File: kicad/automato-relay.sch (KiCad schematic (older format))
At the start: 26 parts, among them J1 Screw_Terminal_01x02, J2 Screw_Terminal_01x02, J3 Screw_Terminal_01x02, J4 Screw_Terminal_01x05, J5 Screw_Terminal_01x02, J6 Screw_Terminal_01x02, J7 Screw_Terminal_01x05, J8 Screw_Terminal_01x02, K1 G5LE-14, K2 G5LE-14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

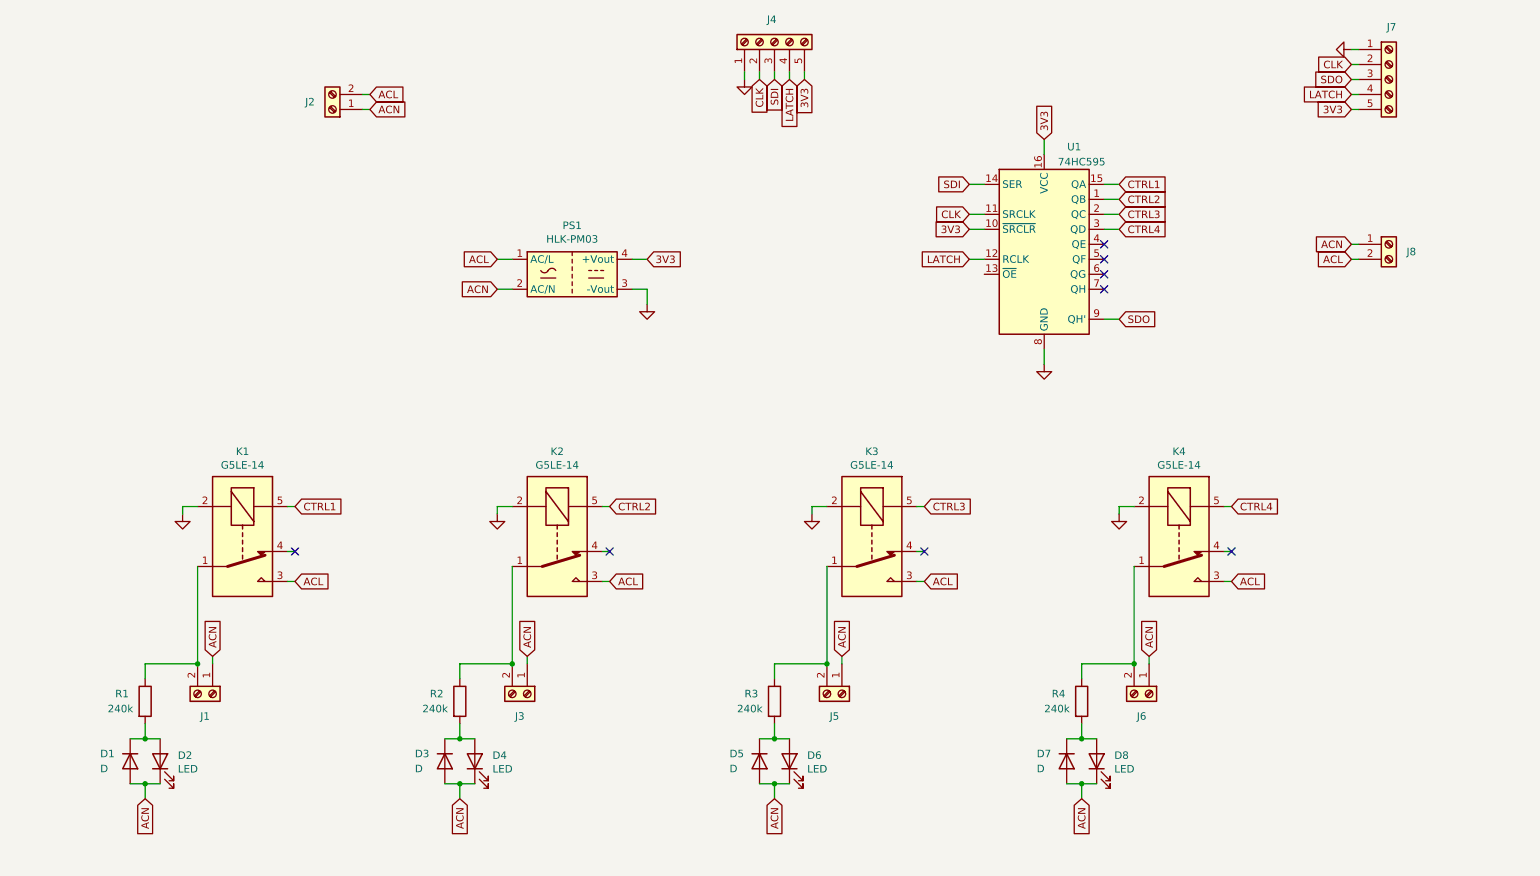
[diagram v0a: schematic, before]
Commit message: add low-side mosfets for relay coils
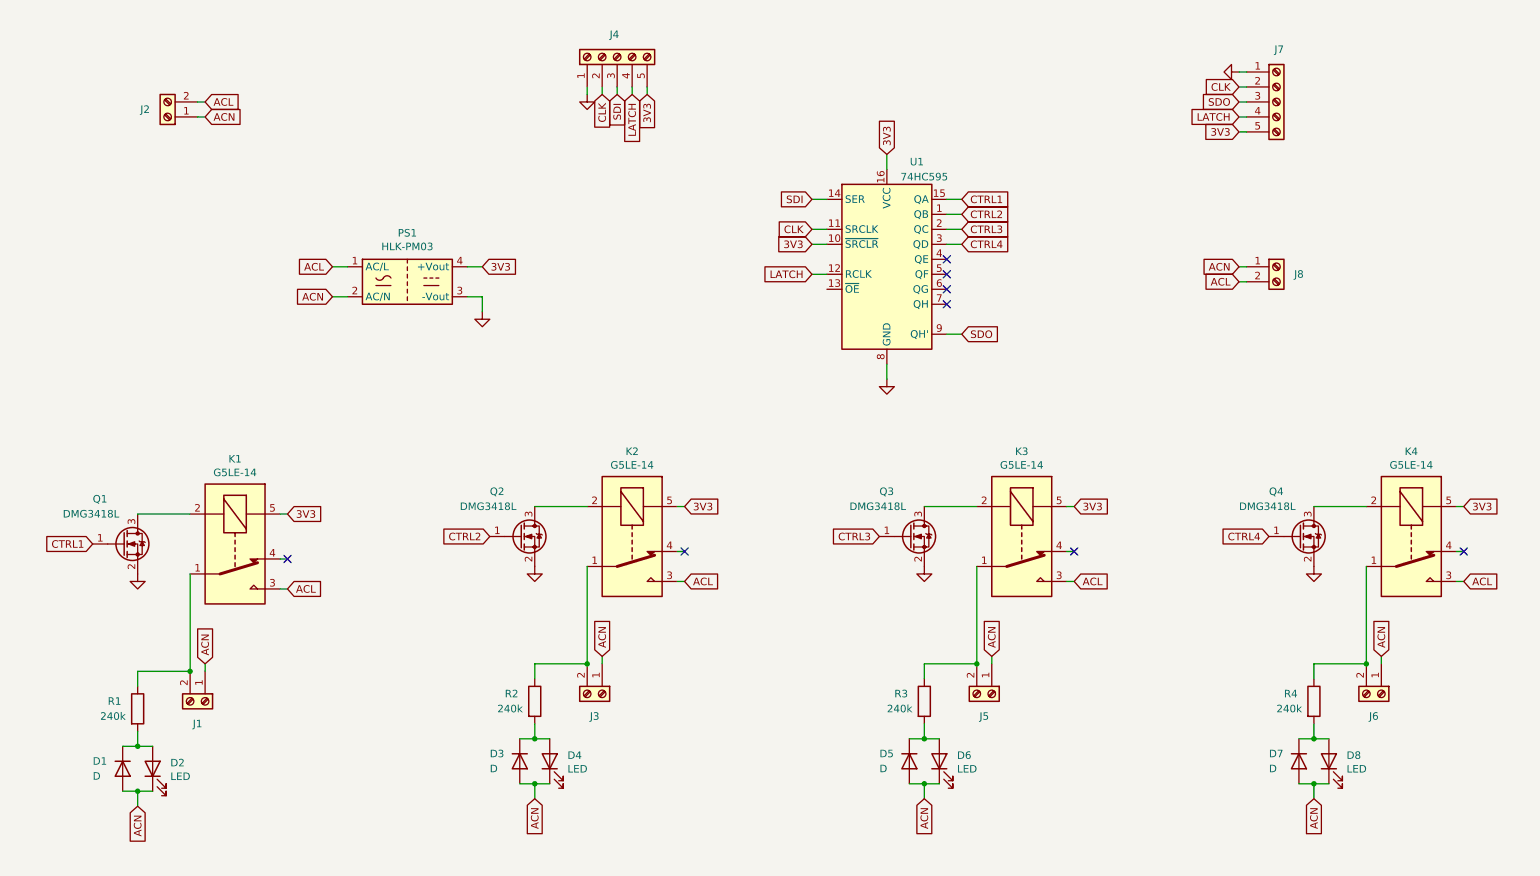
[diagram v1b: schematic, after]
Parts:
- added Q1, Q2, Q3, Q4: DMG3418L, Package_TO_SOT_SMD:SOT-23, symbol Transistor_FET:DMG3418L
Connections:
- net 3V3: now also K1.5, K2.5, K3.5, K4.5
- net CTRL1: now also Q1.1 (G); no longer K1.5
- net CTRL2: now also Q2.1 (G); no longer K2.5
- net CTRL3: now also Q3.1 (G); no longer K3.5
- net CTRL4: now also Q4.1 (G); no longer K4.5
- net GND: now also Q1.2 (S), Q2.2 (S), Q3.2 (S), Q4.2 (S); no longer K1.2, K2.2, K3.2, K4.2
- new net: K1.2, Q1.3 (D)
- new net: K2.2, Q2.3 (D)
- new net: K3.2, Q3.3 (D)
- new net: K4.2, Q4.3 (D)
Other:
- moved on the sheet: D1, D2, D3, D4, D5, D6, D7, D8, J1, J2, J3, J4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

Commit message: add earth ground connections
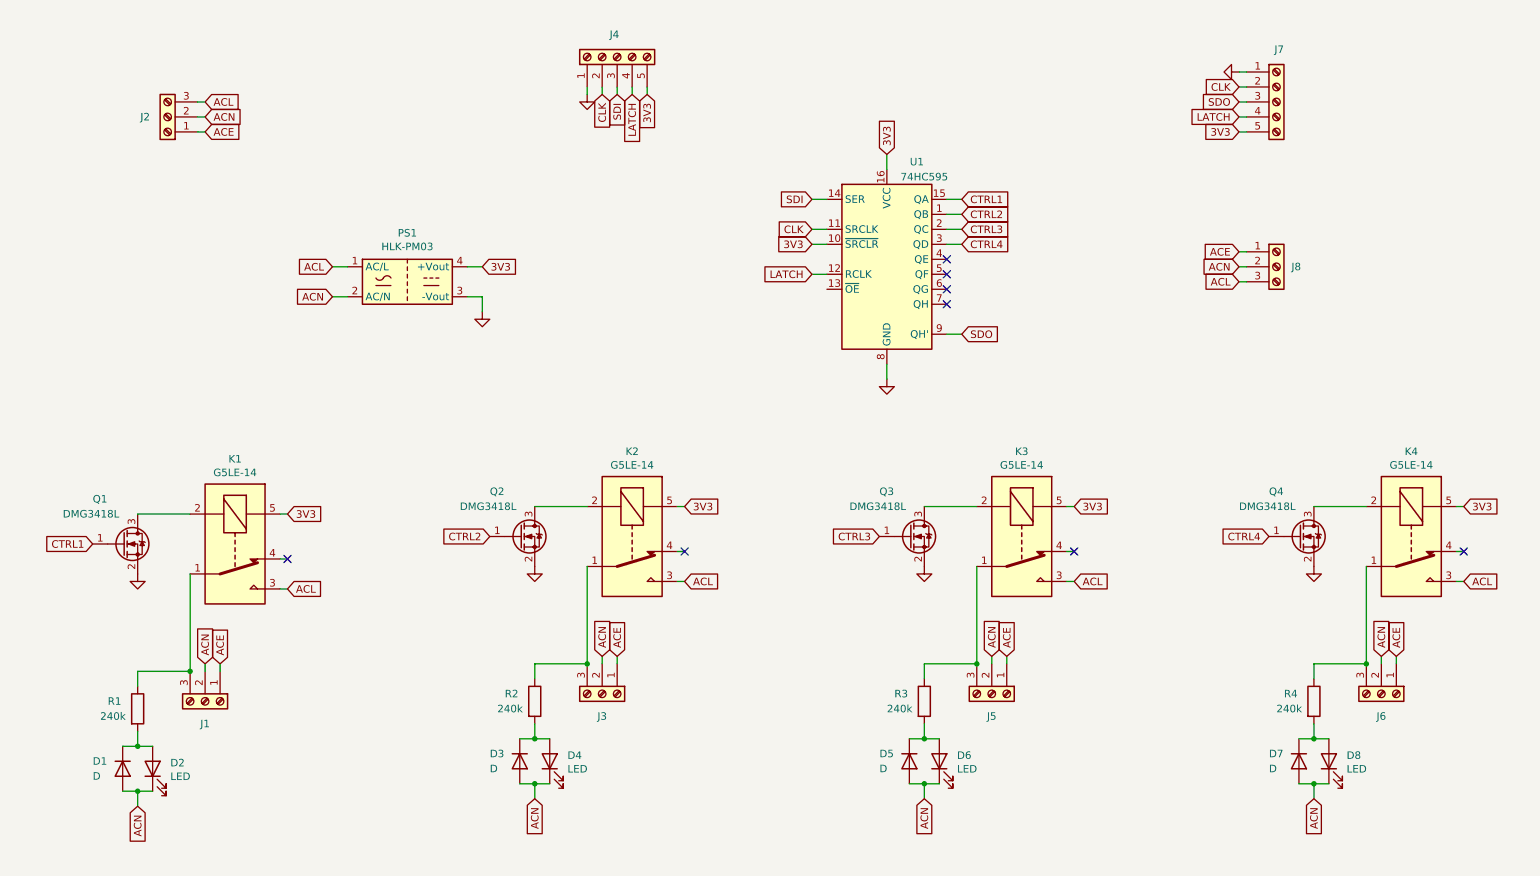
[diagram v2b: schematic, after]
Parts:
- removed J1, J2, J3, J5, J6, J8: Screw_Terminal_01x02, symbol Connector:Screw_Terminal_01x02
- added J1, J2, J3, J5, J6, J8: Screw_Terminal_01x03, symbol Connector:Screw_Terminal_01x03
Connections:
- net ACL: now also J2.3 (Pin_3), J8.3 (Pin_3)
- net ACN: now also J1.2 (Pin_2), J2.2 (Pin_2), J3.2 (Pin_2), J5.2 (Pin_2), J6.2 (Pin_2), J8.2 (Pin_2)
- net at K1.1, R1.1: now also J1.3 (Pin_3)
- net at K2.1, R2.1: now also J3.3 (Pin_3)
- net at K3.1, R3.1: now also J5.3 (Pin_3)
- net at K4.1, R4.1: now also J6.3 (Pin_3)
- new net ACE: J1.1 (Pin_1), J2.1 (Pin_1), J3.1 (Pin_1), J5.1 (Pin_1), J6.1 (Pin_1), J8.1 (Pin_1)
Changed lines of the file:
@@
 Wire Wire Line
 	3800 2350 3900 2350
-$Comp
-L Connector:Screw_Terminal_01x02 J2
-U 1 1 60248A15
-P 1800 1350
-F 0 "J2" H 1950 1300 50  0000 C CNN
-F 1 "Screw_Terminal_01x02" H 2350 1350 50  0001 C CNN
-F 2 "" H 1800 1350 50  0001 C CNN
-F 3 "~" H 1800 1350 50  0001 C CNN
-	1    1800 1350
-	-1   0    0    1
-$EndComp
 Text GLabel 2900 2550 0    50   Input ~ 0
 ACN
 Text GLabel 2050 5000 1    50   Input ~ 0
 ACN
-$Comp
-L Connector:Screw_Terminal_01x02 J1
-U 1 1 6025D31A
-P 2050 5250
-F 0 "J1" V 2200 5200 50  0000 C CNN
-F 1 "Screw_Terminal_01x02" H 2050 5000 50  0001 C CNN
-F 2 "" H 2050 5250 50  0001 C CNN
-F 3 "~" H 2050 5250 50  0001 C CNN
-	1    2050 5250
-	0    1    1    0
-$EndComp
 Wire Wire Line
 	2900 2550 3000 2550
@@
 Text GLabel 4700 4950 1    50   Input ~ 0
 ACN
-$Comp
-L Connector:Screw_Terminal_01x02 J3
-U 1 1 603390E0
-P 4700 5200
-F 0 "J3" V 4850 5150 50  0000 C CNN
-F 1 "Screw_Terminal_01x02" H 4700 4950 50  0001 C CNN
-F 2 "" H 4700 5200 50  0001 C CNN
-F 3 "~" H 4700 5200 50  0001 C CNN
-	1    4700 5200
-	0    1    1    0
-$EndComp
 Wire Wire Line
 	4700 4950 4700 5000
@@
 Wire Wire Line
 	4600 4350 4600 5000
-Connection ~ 4600 5000
 $Comp
 L automato-relay:G5LE-14 K3
@@
 Text GLabel 7300 4950 1    50   Input ~ 0
 ACN
-$Comp
-L Connector:Screw_Terminal_01x02 J5
-U 1 1 603475EE
-P 7300 5200
-F 0 "J5" V 7450 5150 50  0000 C CNN
-F 1 "Screw_Terminal_01x02" H 7300 4950 50  0001 C CNN
-F 2 "" H 7300 5200 50  0001 C CNN
-F 3 "~" H 7300 5200 50  0001 C CNN
-	1    7300 5200
-	0    1    1    0
-$EndComp
 Wire Wire Line
 	7300 4950 7300 5000
@@
 Wire Wire Line
 	7200 4350 7200 5000
-Connection ~ 7200 5000
 $Comp
 L automato-relay:G5LE-14 K4
@@
 Text GLabel 9900 4950 1    50   Input ~ 0
 ACN
-$Comp
-L Connector:Screw_Terminal_01x02 J6
-U 1 1 60347654
-P 9900 5200
-F 0 "J6" V 10050 5150 50  0000 C CNN
-F 1 "Screw_Terminal_01x02" H 9900 4950 50  0001 C CNN
-F 2 "" H 9900 5200 50  0001 C CNN
-F 3 "~" H 9900 5200 50  0001 C CNN
-	1    9900 5200
-	0    1    1    0
-$EndComp
 Wire Wire Line
 	9900 4950 9900 5000
@@
 Wire Wire Line
 	9800 4350 9800 5000
-Connection ~ 9800 5000
-$Comp
-L Connector:Screw_Terminal_01x02 J8
-U 1 1 603A21E6
-P 9200 2350
-F 0 "J8" H 9350 2300 50  0000 C CNN
-F 1 "Screw_Terminal_01x02" H 9750 2350 50  0001 C CNN
-F 2 "" H 9200 2350 50  0001 C CNN
-F 3 "~" H 9200 2350 50  0001 C CNN
-	1    9200 2350
-	1    0    0    -1
-$EndComp
 Text GLabel 8950 2450 0    50   Input ~ 0
 ACL
@@
 Text GLabel 10450 3950 2    50   Input ~ 0
 3V3
+$Comp
+L Connector:Screw_Terminal_01x03 J2
+U 1 1 602EE614
+P 1800 1350
+F 0 "J2" H 1950 1350 50  0000 C CNN
+F 1 "Screw_Terminal_01x03" H 1718 1116 50  0001 C CNN
+F 2 "" H 1800 1350 50  0001 C CNN
+F 3 "~" H 1800 1350 50  0001 C CNN
+	1    1800 1350
+	-1   0    0    1
+$EndComp
+Text GLabel 2050 1450 2    50   Input ~ 0
+ACE
+Wire Wire Line
+	2000 1450 2050 1450
+$Comp
+L Connector:Screw_Terminal_01x03 J8
+U 1 1 602F4469
+P 9200 2350
+F 0 "J8" H 9300 2350 50  0000 L CNN
+F 1 "Screw_Terminal_01x03" H 9280 2301 50  0001 L CNN
+F 2 "" H 9200 2350 50  0001 C CNN
+F 3 "~" H 9200 2350 50  0001 C CNN
+	1    9200 2350
+	1    0    0    -1
+$EndComp
+Text GLabel 8950 2250 0    50   Input ~ 0
+ACE
+Wire Wire Line
+	9000 2250 8950 2250
+$Comp
+L Connector:Screw_Terminal_01x03 J1
+U 1 1 602F9B9B
+P 2050 5250
+F 0 "J1" V 2200 5250 50  0000 C CNN
+F 1 "Screw_Terminal_01x03" H 1968 5016 50  0001 C CNN
+F 2 "" H 2050 5250 50  0001 C CNN
+F 3 "~" H 2050 5250 50  0001 C CNN
+	1    2050 5250
+	0    1    1    0
+$EndComp
+Text GLabel 2150 5000 1    50   Input ~ 0
+ACE
+Wire Wire Line
+	2150 5000 2150 5050
+$Comp
+L Connector:Screw_Terminal_01x03 J3
+U 1 1 602FEF5E
+P 4700 5200
+F 0 "J3" V 4850 5200 50  0000 C CNN
+F 1 "Screw_Terminal_01x03" H 4618 4966 50  0001 C CNN
+F 2 "" H 4700 5200 50  0001 C CNN
+F 3 "~" H 4700 5200 50  0001 C CNN
+	1    4700 5200
+	0    1    1    0
+$EndComp
+Connection ~ 4600 5000
+$Comp
+L Connector:Screw_Terminal_01x03 J5
+U 1 1 602FF7E9
+P 7300 5200
+F 0 "J5" V 7450 5200 50  0000 C CNN
+F 1 "Screw_Terminal_01x03" H 7218 4966 50  0001 C CNN
+F 2 "" H 7300 5200 50  0001 C CNN
+F 3 "~" H 7300 5200 50  0001 C CNN
+	1    7300 5200
+	0    1    1    0
+$EndComp
+Connection ~ 7200 5000
+$Comp
+L Connector:Screw_Terminal_01x03 J6
+U 1 1 60300197
+P 9900 5200
+F 0 "J6" V 10050 5200 50  0000 C CNN
+F 1 "Screw_Terminal_01x03" H 9818 4966 50  0001 C CNN
+F 2 "" H 9900 5200 50  0001 C CNN
+F 3 "~" H 9900 5200 50  0001 C CNN
+	1    9900 5200
+	0    1    1    0
+$EndComp
+Connection ~ 9800 5000
+Text GLabel 4800 4950 1    50   Input ~ 0
+ACE
+Text GLabel 7400 4950 1    50   Input ~ 0
+ACE
+Text GLabel 10000 4950 1    50   Input ~ 0
+ACE
+Wire Wire Line
+	10000 4950 10000 5000
+Wire Wire Line
+	7400 4950 7400 5000
+Wire Wire Line
+	4800 4950 4800 5000
 $EndSCHEMATC
